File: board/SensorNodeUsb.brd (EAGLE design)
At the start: 73 x 22.2 mm, 18 parts, among them X2 USBPCB

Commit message: modify adjust a part name and a part value
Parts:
- R5: value 10k -> 1k
- renumbered AM1117 to AMS1117
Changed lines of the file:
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@@
 <grid distance="0.0125" unitdist="inch" unit="inch" style="dots" multiple="4" display="yes" altdistance="5" altunitdist="mil" altunit="mil"/>
 <layers>
-<layer number="1" name="Top" color="4" fill="1" visible="no" active="yes"/>
-<layer number="16" name="Bottom" color="1" fill="1" visible="yes" active="yes"/>
+<layer number="1" name="Top" color="4" fill="1" visible="yes" active="yes"/>
+<layer number="16" name="Bottom" color="1" fill="1" visible="no" active="yes"/>
 <layer number="17" name="Pads" color="2" fill="1" visible="yes" active="yes"/>
 <layer number="18" name="Vias" color="2" fill="1" visible="yes" active="yes"/>
 <layer number="19" name="Unrouted" color="6" fill="1" visible="yes" active="yes"/>
 <layer number="20" name="Dimension" color="24" fill="1" visible="yes" active="yes"/>
-<layer number="21" name="tPlace" color="7" fill="1" visible="no" active="yes"/>
-<layer number="22" name="bPlace" color="7" fill="1" visible="yes" active="yes"/>
-<layer number="23" name="tOrigins" color="15" fill="1" visible="no" active="yes"/>
-<layer number="24" name="bOrigins" color="15" fill="1" visible="yes" active="yes"/>
-<layer number="25" name="tNames" color="7" fill="1" visible="no" active="yes"/>
-<layer number="26" name="bNames" color="7" fill="1" visible="yes" active="yes"/>
+<layer number="21" name="tPlace" color="7" fill="1" visible="yes" active="yes"/>
+<layer number="22" name="bPlace" color="7" fill="1" visible="no" active="yes"/>
+<layer number="23" name="tOrigins" color="15" fill="1" visible="yes" active="yes"/>
+<layer number="24" name="bOrigins" color="15" fill="1" visible="no" active="yes"/>
+<layer number="25" name="tNames" color="7" fill="1" visible="yes" active="yes"/>
+<layer number="26" name="bNames" color="7" fill="1" visible="no" active="yes"/>
 <layer number="27" name="tValues" color="7" fill="1" visible="no" active="yes"/>
 <layer number="28" name="bValues" color="7" fill="1" visible="no" active="yes"/>
@@
 <layer number="37" name="tTest" color="7" fill="1" visible="no" active="yes"/>
 <layer number="38" name="bTest" color="7" fill="1" visible="no" active="yes"/>
-<layer number="39" name="tKeepout" color="4" fill="11" visible="no" active="yes"/>
-<layer number="40" name="bKeepout" color="1" fill="11" visible="yes" active="yes"/>
-<layer number="41" name="tRestrict" color="4" fill="10" visible="no" active="yes"/>
-<layer number="42" name="bRestrict" color="1" fill="10" visible="yes" active="yes"/>
+<layer number="39" name="tKeepout" color="4" fill="11" visible="yes" active="yes"/>
+<layer number="40" name="bKeepout" color="1" fill="11" visible="no" active="yes"/>
+<layer number="41" name="tRestrict" color="4" fill="10" visible="yes" active="yes"/>
+<layer number="42" name="bRestrict" color="1" fill="10" visible="no" active="yes"/>
 <layer number="43" name="vRestrict" color="2" fill="10" visible="no" active="yes"/>
 <layer number="44" name="Drills" color="7" fill="1" visible="no" active="yes"/>
@@
 <layer number="49" name="Reference" color="7" fill="1" visible="no" active="yes"/>
 <layer number="50" name="dxf" color="7" fill="1" visible="no" active="yes"/>
-<layer number="51" name="tDocu" color="7" fill="1" visible="no" active="yes"/>
-<layer number="52" name="bDocu" color="7" fill="1" visible="yes" active="yes"/>
+<layer number="51" name="tDocu" color="7" fill="1" visible="yes" active="yes"/>
+<layer number="52" name="bDocu" color="7" fill="1" visible="no" active="yes"/>
 <layer number="53" name="tGND_GNDA" color="7" fill="9" visible="no" active="no"/>
 <layer number="54" name="bGND_GNDA" color="1" fill="9" visible="no" active="no"/>
@@
 <attribute name="VALUE" x="23.1775" y="21.6535" size="0.6096" layer="27" font="vector" ratio="20" rot="R180" align="top-center"/>
 </element>
-<element name="AM1117" library="SparkFun-IC-Power" library_urn="urn:adsk.eagle:library:526" package="SOT223" package3d_urn="urn:adsk.eagle:package:39069/1" value="" x="16.51" y="8.5725" smashed="yes" rot="R180">
+<element name="AMS1117" library="SparkFun-IC-Power" library_urn="urn:adsk.eagle:library:526" package="SOT223" package3d_urn="urn:adsk.eagle:package:39069/1" value="" x="16.51" y="8.5725" smashed="yes" rot="R180">
 <attribute name="NAME" x="18.6055" y="3.7465" size="0.8128" layer="25" ratio="20" rot="R180"/>
 <attribute name="PROD_ID" value="VREG-08170" x="16.51" y="8.5725" size="1.778" layer="27" rot="R180" display="off"/>
@@
 <attribute name="VALUE" x="22.225" y="15.875" size="1.27" layer="27" rot="R270"/>
 </element>
-<element name="R5" library="rcl" library_urn="urn:adsk.eagle:library:334" package="M1206" package3d_urn="urn:adsk.eagle:package:23566/2" value="10k" x="24.765" y="9.2075" smashed="yes" rot="R90">
+<element name="R5" library="rcl" library_urn="urn:adsk.eagle:library:334" package="M1206" package3d_urn="urn:adsk.eagle:package:23566/2" value="1k" x="24.765" y="9.2075" smashed="yes" rot="R90">
 <attribute name="NAME" x="26.67" y="8.89" size="0.8128" layer="25" ratio="20" rot="R90"/>
 <attribute name="SPICEPREFIX" value="R" x="24.765" y="9.2075" size="1.778" layer="27" rot="R90" display="off"/>
@@
 <attribute name="VALUE" x="55.3675" y="19.0625" size="1.016" layer="27" rot="R270"/>
 </element>
-<element name="X2" library="usb" package="USB-A-PCB" value="USBPCB" x="5.08" y="11.43" smashed="yes">
-<attribute name="NAME" x="9.38" y="3.635" size="1.27" layer="25"/>
-</element>
+<element name="X2" library="usb" package="USB-A-PCB" value="USBPCB" x="5.08" y="11.43" smashed="yes"/>
 <element name="BME280/SI7021" library="thomo" package="TEMP-HUM-PRES-BME280" value="TEMP-HUM-PRES-BME280" x="66.04" y="14.9225" smashed="yes">
 <attribute name="NAME" x="64.135" y="20.6375" size="0.8128" layer="25" ratio="20" align="bottom-center"/>
@@
 <contactref element="ESP-12E" pad="9"/>
 <contactref element="ESP-12E" pad="10"/>
-<contactref element="AM1117" pad="1"/>
+<contactref element="AMS1117" pad="1"/>
 <contactref element="C2" pad="2"/>
 <contactref element="JP2" pad="4"/>
@@
 <contactref element="R3" pad="2"/>
 <contactref element="R4" pad="2"/>
-<contactref element="AM1117" pad="4"/>
-<contactref element="AM1117" pad="2"/>
+<contactref element="AMS1117" pad="4"/>
+<contactref element="AMS1117" pad="2"/>
 <contactref element="C2" pad="1"/>
 <contactref element="SHOTTKY" pad="C"/>
@@
 <signal name="N$8">
 <contactref element="C1" pad="1"/>
-<contactref element="AM1117" pad="3"/>
+<contactref element="AMS1117" pad="3"/>
 <contactref element="X2" pad="5V"/>
 <wire x1="4.88" y1="7.93" x2="13.01" y2="7.93" width="0.8128" layer="1"/>

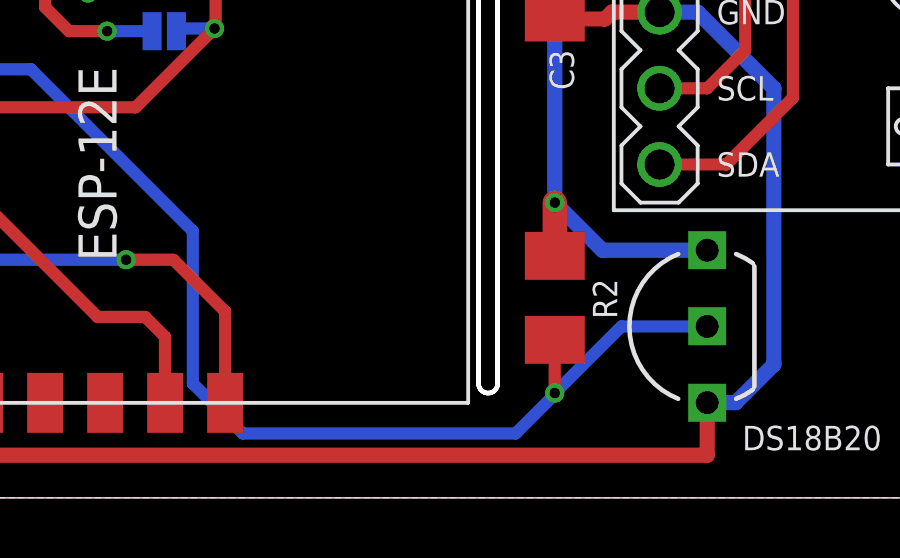
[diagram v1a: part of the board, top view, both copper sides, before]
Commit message: remove 2 vias near R2
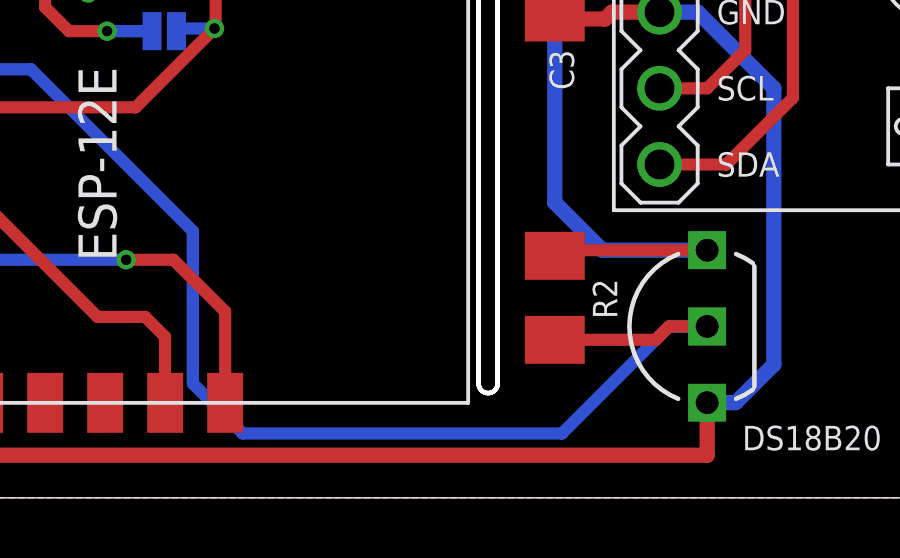
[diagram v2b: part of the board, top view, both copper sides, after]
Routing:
- net DATA_1W: track 43.8 -> 47.3 mm, vias 2 -> 1
- net +3V3: track 103.3 -> 106.7 mm, vias 6 -> 5
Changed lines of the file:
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@@
 <layers>
 <layer number="1" name="Top" color="4" fill="1" visible="yes" active="yes"/>
-<layer number="16" name="Bottom" color="1" fill="1" visible="no" active="yes"/>
+<layer number="16" name="Bottom" color="1" fill="1" visible="yes" active="yes"/>
 <layer number="17" name="Pads" color="2" fill="1" visible="yes" active="yes"/>
 <layer number="18" name="Vias" color="2" fill="1" visible="yes" active="yes"/>
@@
 <wire x1="62.5475" y1="8.255" x2="59.055" y2="8.255" width="0.508" layer="16"/>
 <wire x1="59.055" y1="8.255" x2="57.4675" y2="9.8425" width="0.508" layer="16"/>
-<via x="57.4675" y="9.8425" extent="1-16" drill="0.35"/>
-<wire x1="57.4675" y1="9.8425" x2="57.4675" y2="8.0675" width="0.8128" layer="1"/>
 <wire x1="57.4675" y1="9.8425" x2="57.4675" y2="17.145" width="0.508" layer="16"/>
 <wire x1="59.055" y1="18.7325" x2="60.96" y2="18.7325" width="0.508" layer="16"/>
@@
 <wire x1="19.685" y1="18.66" x2="21.0275" y2="20.0025" width="0.8128" layer="1"/>
 <contactref element="BME280/SI7021" pad="1"/>
+<wire x1="57.4675" y1="8.0675" x2="57.655" y2="8.255" width="0.4064" layer="1"/>
+<wire x1="57.655" y1="8.255" x2="62.5475" y2="8.255" width="0.4064" layer="1"/>
 </signal>
 <signal name="N$1">
@@
 <wire x1="45.4025" y1="8.89" x2="40.005" y2="14.2875" width="0.4064" layer="16"/>
 <wire x1="40.005" y1="14.2875" x2="35.56" y2="14.2875" width="0.4064" layer="16"/>
-<wire x1="62.5475" y1="5.715" x2="59.69" y2="5.715" width="0.4064" layer="16"/>
-<wire x1="59.69" y1="5.715" x2="57.4675" y2="3.4925" width="0.4064" layer="16"/>
-<via x="57.4675" y="3.4925" extent="1-16" drill="0.35"/>
-<wire x1="57.4675" y1="3.4925" x2="57.4675" y2="5.2675" width="0.4064" layer="1"/>
-<wire x1="57.4675" y1="3.4925" x2="57.4675" y2="3.44905" width="0.4064" layer="16"/>
-<wire x1="57.4675" y1="3.44905" x2="56.16475" y2="2.1463" width="0.4064" layer="16"/>
-<wire x1="56.16475" y1="2.1463" x2="47.0662" y2="2.1463" width="0.4064" layer="16"/>
-<wire x1="47.0662" y1="2.1463" x2="45.4025" y2="3.81" width="0.4064" layer="16"/>
+<wire x1="45.4025" y1="3.81" x2="47.0662" y2="2.1463" width="0.4064" layer="16"/>
 <wire x1="34.48" y1="19.3675" x2="34.48" y2="17.59" width="0.4064" layer="1"/>
 <wire x1="35.56" y1="16.51" x2="35.56" y2="14.2875" width="0.4064" layer="1"/>
 <wire x1="35.56" y1="16.51" x2="34.48" y2="17.59" width="0.4064" layer="1"/>
 <via x="35.56" y="14.2875" extent="1-16" drill="0.35"/>
+<wire x1="61.2775" y1="5.715" x2="62.5475" y2="5.715" width="0.4064" layer="16"/>
+<wire x1="47.0662" y1="2.1463" x2="57.7088" y2="2.1463" width="0.4064" layer="16"/>
+<wire x1="57.7088" y1="2.1463" x2="61.2775" y2="5.715" width="0.4064" layer="16"/>
+<wire x1="57.4675" y1="5.2675" x2="60.83" y2="5.2675" width="0.4064" layer="1"/>
+<wire x1="60.83" y1="5.2675" x2="61.2775" y2="5.715" width="0.4064" layer="1"/>
+<wire x1="61.2775" y1="5.715" x2="62.5475" y2="5.715" width="0.4064" layer="1"/>
 </signal>
 <signal name="N$3">

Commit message: 5-pin programming interface
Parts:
- removed C4: 2.2uF, rcl:C1206
- removed JP2: ISP, jumper:JP4
- removed RST: (no value), wirepad:2,15/1,0
- removed SHOTTKY: Shottky, SparkFun-DiscreteSemi:SMA-DIODE
- added J1: JP5E, thomo:JP5
- R5: value 1k -> 10k
- moved R1 5.32 mm to (26.7, 16.2), turned to 0 degrees
- moved R3 5.24 mm to (26.7, 19.7), turned to 180 degrees
- moved R4 3.42 mm to (26.7, 12.4), turned to 180 degrees
- moved C2 3.19 mm to (21.9, 12.4), turned to 90 degrees
- moved R5 2.01 mm to (26.7, 8.57), turned to 0 degrees
- moved AMS1117 1.93 mm to (16.8, 10.5)
- moved C1 1.62 mm to (17.8, 16.8)
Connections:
- removed net N$1: C4.1, ESP-12E.1, R1.2, RST.1, SHOTTKY.A, WAKEUP.2
- removed net N$4: ESP-12E.12, R4.1
- removed net N$5: C4.2, JP2.1, R5.2
- removed net N$6: ESP-12E.16, JP2.2
- removed net N$7: ESP-12E.15, JP2.3
- new net DTR: ESP-12E.12, J1.1, R4.1
- new net N$9: ESP-12E.10, R5.2
- new net RST: ESP-12E.1, J1.2, R1.2, WAKEUP.2
- new net RX: ESP-12E.15, J1.4
- new net TX: ESP-12E.16, J1.3
- net +3V3: no longer SHOTTKY.C
- net GND: now also J1.5; no longer ESP-12E.10, JP2.4
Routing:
- net N$1: track 40.7 -> 0.00 mm, vias 1 -> 0
- net RST: track 0.00 -> 38.2 mm, vias 0 -> 2
- net TX: track 0.00 -> 31.7 mm, vias 0 -> 1
- net RX: track 0.00 -> 30.7 mm
- net N$7: track 28.4 -> 0.00 mm, vias 1 -> 0
- net DTR: track 0.00 -> 27.5 mm, vias 0 -> 2
- net N$6: track 26.6 -> 0.00 mm, vias 1 -> 0
- net +3V3: track 106.7 -> 88.4 mm, vias 5 -> 1
- net N$4: track 14.3 -> 0.00 mm
- net N$5: track 11.5 -> 0.00 mm
- net N$9: track 0.00 -> 10.2 mm, vias 0 -> 2
- net I2C_SDA: track 40.5 -> 31.6 mm
- net N$3: track 17.2 -> 21.3 mm, vias 2 -> 0
- net GND: track 105.2 -> 106.8 mm
- net DATA_1W: track 47.3 -> 46.0 mm
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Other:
- board text added: "RST"
- board text added: "SensorNode v1.1 ThoMo 07/2019"
- board text removed: "SensorNode ThoMo 04/2019"

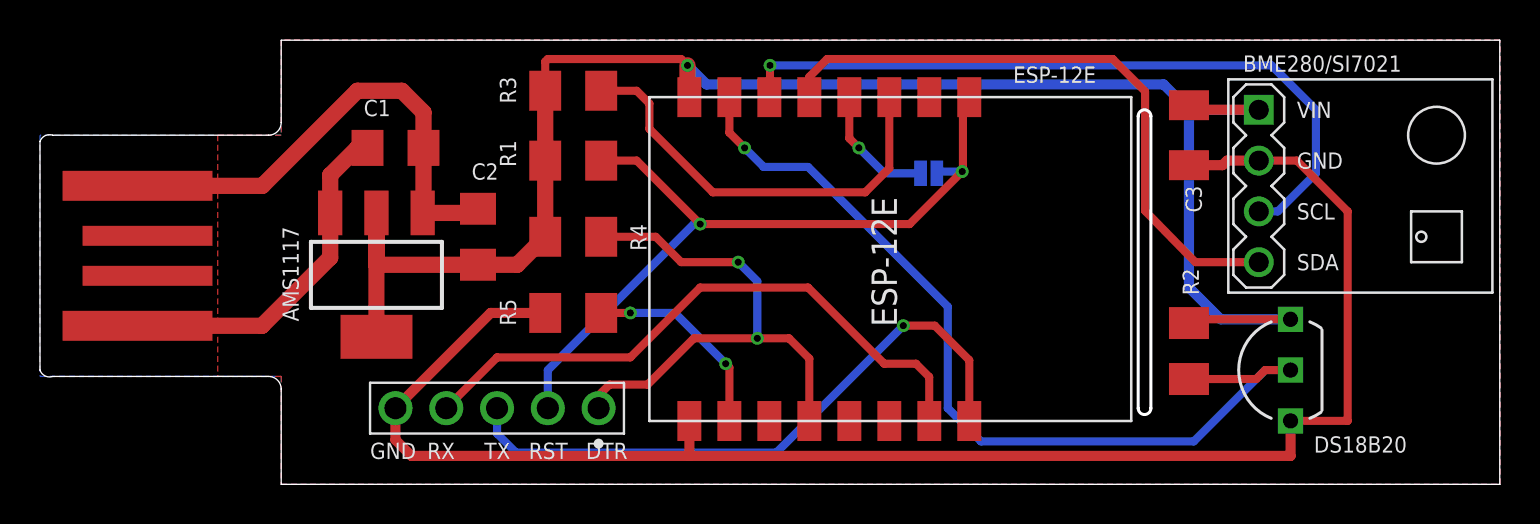
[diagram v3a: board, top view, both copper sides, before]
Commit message: change programming interface
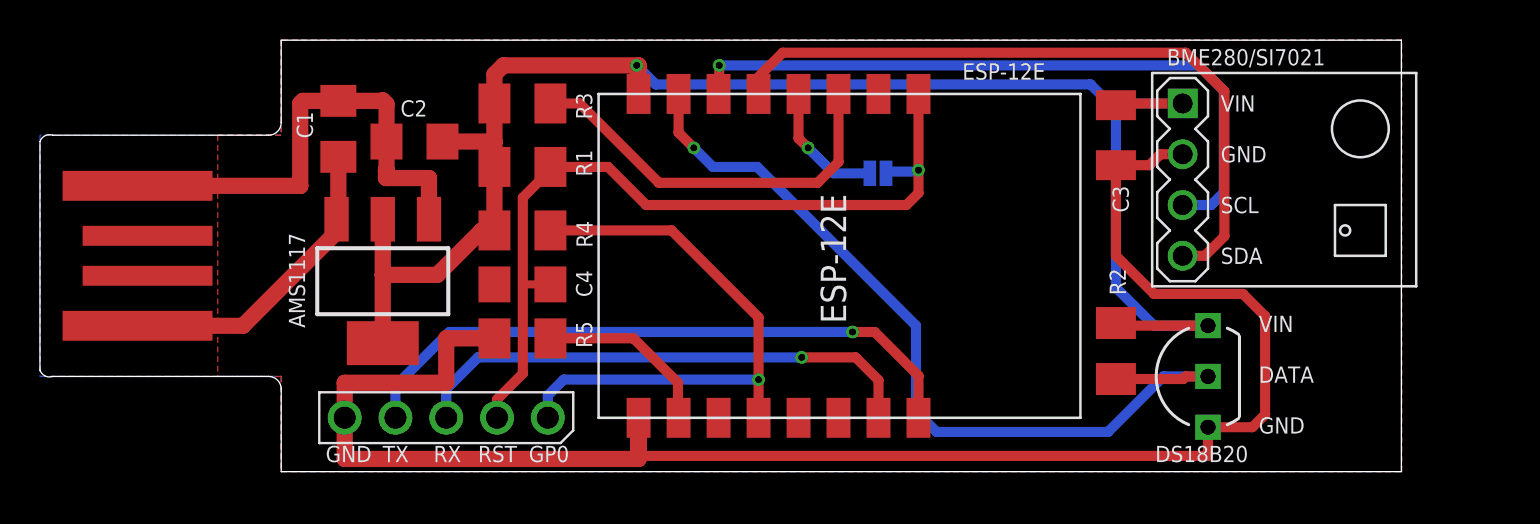
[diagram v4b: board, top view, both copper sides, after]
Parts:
- added C4: 1nF, rcl:C1206
- DS18B20: device thomo:21-0248A -> thomo:TO-92
- moved C2 5.72 mm to (18.7, 17.1), turned to 180 degrees
- moved DS18B20 4.14 mm to (58.4, 7.94)
- moved BME280/SI7021 3.82 mm to (62.2, 15.2)
- moved C3 3.65 mm to (53.8, 17.5)
- moved R2 3.65 mm to (53.8, 6.67)
- moved C1 3.01 mm to (14.9, 17.8), turned to 90 degrees
- moved R5 2.84 mm to (24.1, 7.30)
- moved R3 2.62 mm to (24.1, 19.1)
- moved J1 2.58 mm to (25.4, 3.33)
- moved R1 2.56 mm to (24.1, 15.9)
- moved R4 2.56 mm to (24.1, 12.7)
- moved ESP-12E 2.54 mm to (38.1, 11.9)
- moved WAKEUP 2.54 mm to (41.9, 15.6)
- moved AMS1117 0.45 mm to (17.1, 10.2)
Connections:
- net DTR renamed GP0
- removed net RX: ESP-12E.15, J1.4
- removed net TX: ESP-12E.16, J1.3
- new net N$1: ESP-12E.15, J1.3
- new net N$4: ESP-12E.16, J1.4
- net GND: now also C4.1
- net RST: now also C4.2
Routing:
- net N$4: track 0.00 -> 31.9 mm, vias 0 -> 1
- net TX: track 31.7 -> 0.00 mm, vias 1 -> 0
- net RX: track 30.7 -> 0.00 mm
- net N$1: track 0.00 -> 26.1 mm, vias 0 -> 1
- net GND: track 106.8 -> 111.6 mm
- net +3V3: track 88.4 -> 84.3 mm
- net I2C_SDA: track 31.6 -> 35.2 mm
- net DATA_1W: track 46.0 -> 42.9 mm
- net RST: track 38.2 -> 41.1 mm, vias 2 -> 1
- net I2C_SCL: track 36.6 -> 34.6 mm
- net N$8: track 17.6 -> 15.7 mm
- net GP0: track 27.5 -> 29.2 mm, vias 2 -> 1
- net N$3: track 21.3 -> 19.9 mm
- net N$9: track 10.2 -> 9.07 mm, vias 2 -> 0
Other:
- board size 73 x 22.2 mm -> 68.1 x 21.6 mm
- board text added: "DATA"
- board text added: "GP0"
- board text added: "SensorNode v2.0 ThoMo 07/2019"
- board text added: "VIN"
- board text removed: "DTR"
- board text removed: "SensorNode v1.1 ThoMo 07/2019"
